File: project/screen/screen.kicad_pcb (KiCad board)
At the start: 4 copper layers, 41.9 x 30 mm, 34 parts, among them J1 USB_C_Receptacle_USB2.0, J2 Conn_01x06_Female, J3 Conn_01x02_Female, J4 Conn_01x12_Female, SW1 SW_Push, SW2 SW_Push, SW3 SW_DPDT_x2, U1 ESP-12E, U2 TP4056_[C16581], U3 SPX3819M5-L-3-3

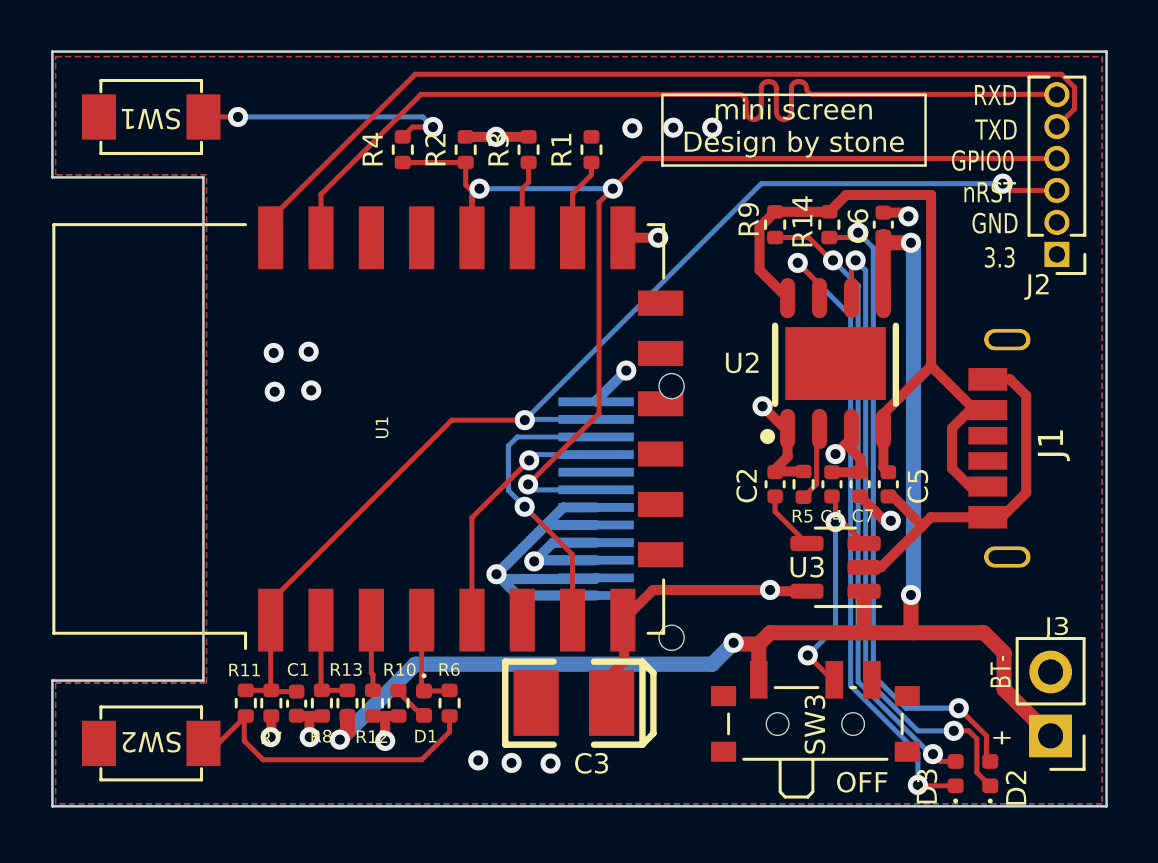
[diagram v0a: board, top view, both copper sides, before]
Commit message: fix: screen rst and cs
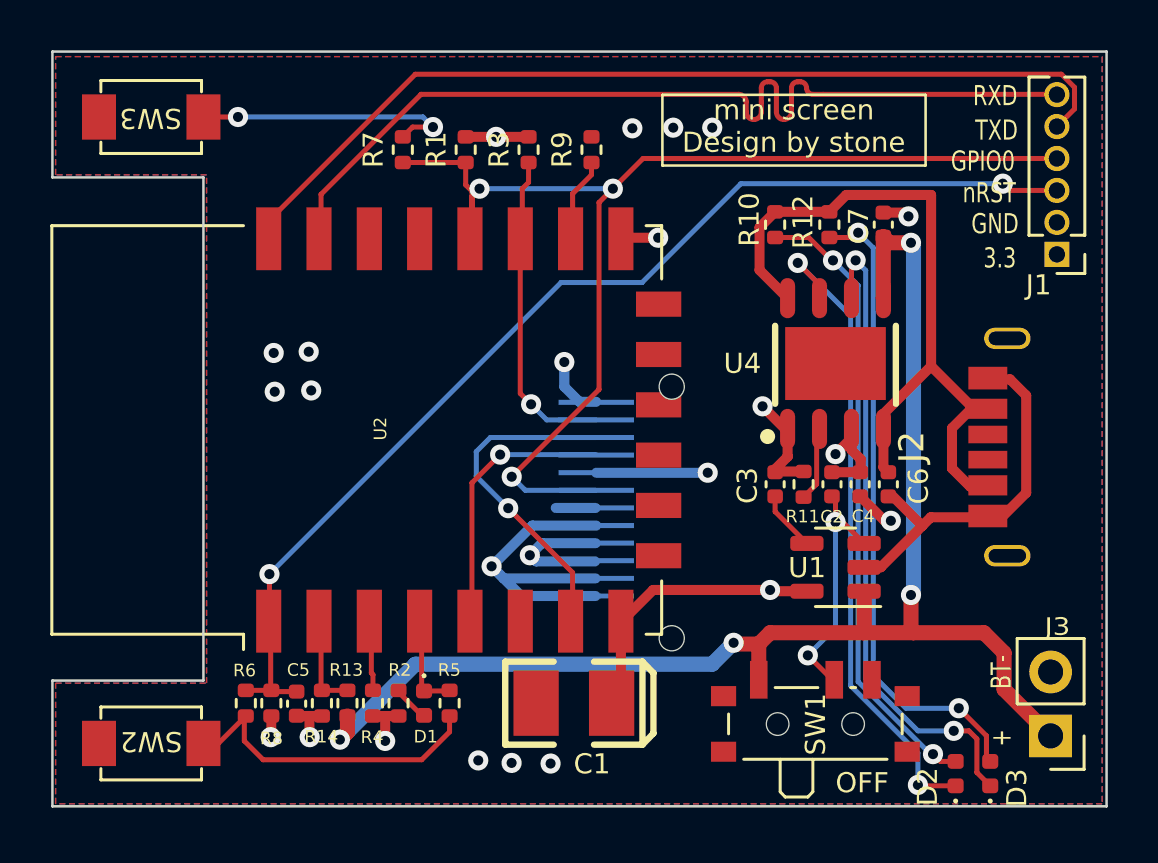
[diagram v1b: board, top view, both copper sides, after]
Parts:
- removed the J1 at (135.4, 51.5)
- removed J4: Conn_01x12_Female, My-lib:TFT_1.4_12_front
- added J2: USB_C_6pin, My-lib-footprints:USB_C_6pin, F.Cu at (135.4, 51.4)
- added U3: TFT_1.3_12, My-lib-footprints:TFT_1.3_12_front, B.Cu at (113.0, 50.7)
- R11: renamed from R5; value 1.2K -> 2K
- R13: value 10k -> 100k
- R14: renamed from R8; value 10k -> 100k
- R4: renamed from R12; value 12k -> 12K
- moved U2 0.09 mm to (109.6, 50.7)
- renumbered C3 to C1, C4 to C2, C2 to C3, C7 to C4, C1 to C5, C5 to C6, C6 to C7, D3 to D2, D2 to D3, J2 to J1, R2 to R1, R9 to R10, R14 to R12, R10 to R2, R6 to R5, R11 to R6, R4 to R7, R7 to R8, R1 to R9, SW3 to SW1, SW1 to SW3, U3 to U1, U1 to U2, U2 to U4
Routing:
- net /GPIO2: track 3.09 -> 12.7 mm, vias 0 -> 1
- net GND: track 47.9 -> 50.3 mm, vias 17 -> 18
- net /nRST: track 46.7 -> 44.6 mm
- net /GPIO13: track 11.6 -> 13.3 mm
- net /GPIO14: track 10.0 -> 10.9 mm
- net /GPIO0: track 47.1 -> 47.8 mm

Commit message: feat: update screen  v1.3
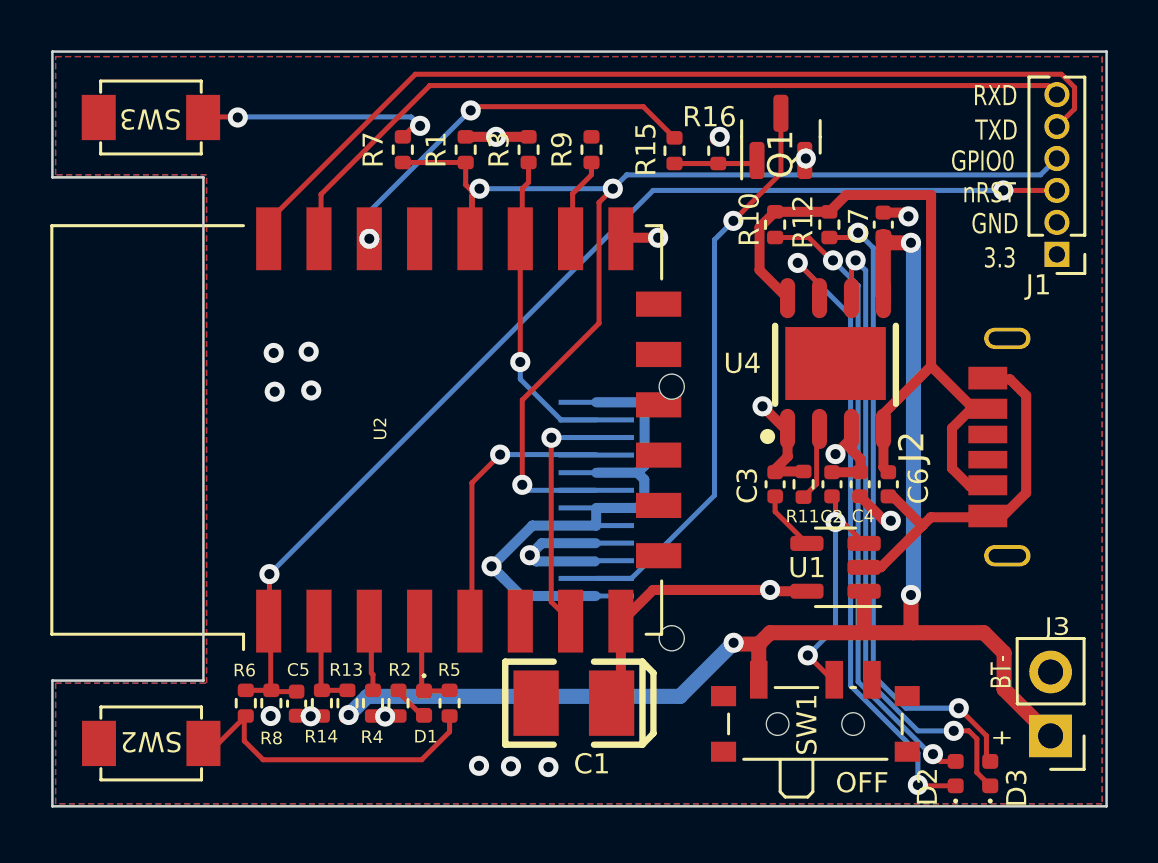
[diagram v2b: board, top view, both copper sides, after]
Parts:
- added Q1: S8050, Package_TO_SOT_SMD:SOT-23, F.Cu at (126.5, 39.1)
- added R15: 1K, Resistor_SMD:R_0402_1005Metric, F.Cu at (122.2, 39.6)
- added R16: 12K, Resistor_SMD:R_0402_1005Metric, F.Cu at (124.0, 39.6)
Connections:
- U3 pad 2: GND -> Net-(U3-Pad2)
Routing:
- net Net-(U3-Pad2): track 0.00 -> 22.3 mm, vias 0 -> 1
- net /GPIO5: track 0.00 -> 15.5 mm, vias 0 -> 2
- net /RXD: track 37.3 -> 32.9 mm
- net /GPIO13: track 13.3 -> 9.40 mm
- net Net-(Q1-Pad1): track 0.00 -> 3.33 mm
- net GND: track 50.3 -> 47.8 mm, vias 18 -> 14
- net +BATT: track 56.0 -> 54.3 mm
- net +3V3: track 23.7 -> 22.0 mm, vias 6 -> 7
- net Net-(R7-Pad2): track 10.7 -> 9.63 mm
